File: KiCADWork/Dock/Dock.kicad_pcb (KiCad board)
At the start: 2 copper layers, 166.3 x 101.1 mm, 11 parts, among them J1 Conn_01x10_Pin, J2 Conn_01x10_Pin, U1 MCP73831T-2ACI/OT, U2 XB6096I2SV

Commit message: Dock Updates
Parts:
- removed J2: Conn_01x10_Pin, easyeda2kicad:HDR-TH_10P-P1.27-H-M-R2-C7-S1.27-W7.5-N
- removed U2: XB6096I2SV, easyeda2kicad:WDFN-6_L2.0-W2.0-P0.65-BL-EP
- added BT1: Battery, easyeda2kicad:CONN-TH_S2B-PH-K-LF-SN, B.Cu at (124.1, 52.7)
- added C10: 100n, Capacitor_SMD:C_0402_1005Metric_Pad0.74x0.62mm_HandSolder, F.Cu at (152.9, 61.1)
- added C11: 1u, Capacitor_SMD:C_0402_1005Metric_Pad0.74x0.62mm_HandSolder, F.Cu at (152.9, 63.1)
- added C4: 1u, Capacitor_SMD:C_0402_1005Metric_Pad0.74x0.62mm_HandSolder, F.Cu at (152.9, 53.2)
- added C7: 100n, Capacitor_SMD:C_0402_1005Metric_Pad0.74x0.62mm_HandSolder, F.Cu at (152.9, 55.2)
- added C8: 1u, Capacitor_SMD:C_0402_1005Metric_Pad0.74x0.62mm_HandSolder, F.Cu at (152.9, 57.1)
- added C9: 100n, Capacitor_SMD:C_0402_1005Metric_Pad0.74x0.62mm_HandSolder, F.Cu at (152.9, 59.1)
- added D2: LED, LED_SMD:LED_0603_1608Metric_Pad1.05x0.95mm_HandSolder, F.Cu at (145.1, 51.1)
- added J3: USB_C_Receptacle, easyeda2kicad:USB-C-SMD_TYPEC-952-ACP24, F.Cu at (186.6, 61.1)
- added J4: Conn_01x10_Socket, easyeda2kicad:HDR-TH_10P-P1.27-V-M-R2-C5-S1.27-1, B.Cu at (125.8, 39.1)
- added P1: USB_C_Plug, easyeda2kicad:USB-C-SMD_TYPEC-952-ACP24, F.Cu at (186.6, 44.5)
- added Q1: NTJD4152PT1G, easyeda2kicad:SC-88-6_L2.0-W1.3-P0.65-LS2.1-BL, F.Cu at (156.7, 46.0)
- added R10: 2k, Resistor_SMD:R_0402_1005Metric_Pad0.72x0.64mm_HandSolder, F.Cu at (153.0, 49.1)
- added R11: 2k, Resistor_SMD:R_0402_1005Metric_Pad0.72x0.64mm_HandSolder, F.Cu at (153.0, 51.1)
- added R12: 220, Resistor_SMD:R_0402_1005Metric_Pad0.72x0.64mm_HandSolder, F.Cu at (148.9, 48.2)
- added R13: 220, Resistor_SMD:R_0402_1005Metric_Pad0.72x0.64mm_HandSolder, F.Cu at (148.9, 50.2)
- added R4: 5k1, Resistor_SMD:R_0402_1005Metric_Pad0.72x0.64mm_HandSolder, F.Cu at (159.9, 45.1)
- added R5: 5k1, Resistor_SMD:R_0402_1005Metric_Pad0.72x0.64mm_HandSolder, F.Cu at (159.9, 47.0)
- added R6: 100, Resistor_SMD:R_0402_1005Metric_Pad0.72x0.64mm_HandSolder, F.Cu at (156.2, 53.2)
- added R7: 100, Resistor_SMD:R_0402_1005Metric_Pad0.72x0.64mm_HandSolder, F.Cu at (159.3, 53.2)
- added R8: 100, Resistor_SMD:R_0402_1005Metric_Pad0.72x0.64mm_HandSolder, F.Cu at (153.0, 45.1)
- added R9: 12k 1%, Resistor_SMD:R_0402_1005Metric_Pad0.72x0.64mm_HandSolder, F.Cu at (153.0, 47.1)
- added Y1: X322524MOB4SI, easyeda2kicad:CRYSTAL-SMD_4P-L3.2-W2.5-BL, F.Cu at (157.4, 58.5)
- C1: value 10u -> 18p
- C2: value 100n -> 18p
- C3: value 10u -> 100n
- D1: value WHITE LED -> LED
- J1: value Conn_01x10_Pin -> USB_C_Receptacle; footprint easyeda2kicad:HDR-TH_10P-P1.27-H-M-R2-C7-S1.27-W7.5-N -> easyeda2kicad:TYPE-C-SMD_C9900025773
- R1: value 2k -> 100
- R3: value 2k -> 10k
- U1: value MCP73831T-2ACI/OT -> USB2422T-I/MJ; footprint easyeda2kicad:SOT-23-5_L3.0-W1.7-P0.95-LS2.8-BL -> Temp:QFN-24_L4.0-W4.0-P0.50-TL-EP2.5
- moved J1 43.4 mm to (127.0, 52.8), turned to -90 degrees
- moved D1 24.9 mm to (145.1, 48.5)
- moved U1 5.04 mm to (168.5, 54.6)
- moved R3 1.98 mm to (161.6, 64.3)
- moved R1 1.98 mm to (161.6, 60.4)
- moved R2 1.98 mm to (161.6, 62.3)
- moved C1 1.98 mm to (164.9, 60.3)
- moved C2 1.98 mm to (164.9, 62.3)
- moved C3 1.98 mm to (164.9, 64.3)
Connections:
- C1 pad 1: +BATT -> GND
- C1 pad 2: GND -> Net-(U1-XTALIN/CLKIN)
- C2 pad 1: Net-(U2-VDD) -> Net-(U1-XTALOUT/(CLKIN_EN))
- C2 pad 2: /Charging/BATGND -> GND
- C3 pad 1: /Charging/VBUS -> GND
- C3 pad 2: GND -> +3V3
- D1 pad 1: Net-(D1-K) -> GND
- D1 pad 2: /Charging/VBUS -> Net-(D1-A)
- J1 pad 1: unconnected-(J1-Pin_1-Pad1) -> (no net)
- J1 pad 2: unconnected-(J1-Pin_2-Pad2) -> (no net)
- J1 pad 3: unconnected-(J1-Pin_3-Pad3) -> (no net)
- J1 pad 4: unconnected-(J1-Pin_4-Pad4) -> (no net)
- R1 pad 1: Net-(D1-K) -> Net-(U1-VBUS_DET)
- R1 pad 2: Net-(U1-STAT) -> VTRef
- R2 pad 1: Net-(U2-VDD) -> GND
- R2 pad 2: +BATT -> Net-(U1-VBUS_DET)
- R3 pad 1: Net-(U1-PROG) -> RESET
- R3 pad 2: GND -> +3V3
- U1 pad 1: Net-(U1-STAT) -> +3V3
- U1 pad 2: GND -> /DeviceSelect/D1-
- U1 pad 3: +BATT -> /DeviceSelect/D1+
- U1 pad 4: /Charging/VBUS -> /DeviceSelect/D2-
- U1 pad 5: Net-(U1-PROG) -> /DeviceSelect/D2+
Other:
- board size 166.3 x 101.1 mm -> 70.5 x 35.5 mm

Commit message: Ignoring Backups
More Dock progress
All local backups removed
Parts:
- removed BT1: Battery, easyeda2kicad:CONN-TH_S2B-PH-K-LF-SN
- removed J3: USB_C_Receptacle, easyeda2kicad:USB-C-SMD_TYPEC-952-ACP24
- added BT2: Battery, easyeda2kicad:CONN-TH_S2B-PH-K-LF-SN, B.Cu at (124.1, 52.7)
- added C12: 4.7u, Capacitor_SMD:C_0402_1005Metric_Pad0.74x0.62mm_HandSolder, F.Cu at (115.2, 37.4)
- added C13: 2.2u, Capacitor_SMD:C_0402_1005Metric_Pad0.74x0.62mm_HandSolder, F.Cu at (143.8, 21.6)
- added C14: 2.2u, Capacitor_SMD:C_0402_1005Metric_Pad0.74x0.62mm_HandSolder, F.Cu at (131.0, 21.7)
- added C15: 10u, Capacitor_SMD:C_0402_1005Metric_Pad0.74x0.62mm_HandSolder, F.Cu at (100.6, 77.5)
- added C16: 22u, Capacitor_SMD:C_0603_1608Metric_Pad1.08x0.95mm_HandSolder, F.Cu at (96.9, 78.5)
- added C17: 22u, Capacitor_SMD:C_0603_1608Metric_Pad1.08x0.95mm_HandSolder, F.Cu at (96.9, 81.0)
- added C5: 1u, Capacitor_SMD:C_0402_1005Metric_Pad0.74x0.62mm_HandSolder, F.Cu at (107.9, 30.8)
- added C6: 4.7u, Capacitor_SMD:C_0402_1005Metric_Pad0.74x0.62mm_HandSolder, F.Cu at (115.2, 35.4)
- added D3: BLUE LED, LED_SMD:LED_0603_1608Metric_Pad1.05x0.95mm_HandSolder, F.Cu at (110.6, 26.7)
- added D4: BLUE RED, LED_SMD:LED_0603_1608Metric_Pad1.05x0.95mm_HandSolder, F.Cu at (104.0, 29.0)
- added L1: 4.7u, easyeda2kicad:IND-SMD_L5.2-W5.2_YSPI0530, F.Cu at (95.3, 73.7)
- added P2: USB_C_Plug, easyeda2kicad:USB-C-SMD_918-118A2021S40003, F.Cu at (191.8, 65.3)
- added R14: 1.78k, Resistor_SMD:R_0402_1005Metric_Pad0.72x0.64mm_HandSolder, F.Cu at (98.9, 28.6)
- added R15: 1.18k, Resistor_SMD:R_0402_1005Metric_Pad0.72x0.64mm_HandSolder, F.Cu at (98.9, 30.6)
- added R16: 1.18k, Resistor_SMD:R_0402_1005Metric_Pad0.72x0.64mm_HandSolder, F.Cu at (98.9, 32.6)
- added R17: 1.18k, Resistor_SMD:R_0402_1005Metric_Pad0.72x0.64mm_HandSolder, F.Cu at (104.1, 31.5)
- added R18: 10k, Resistor_SMD:R_0402_1005Metric_Pad0.72x0.64mm_HandSolder, F.Cu at (107.7, 39.1)
- added R19: 100k, Resistor_SMD:R_0402_1005Metric_Pad0.72x0.64mm_HandSolder, F.Cu at (104.5, 78.1)
- added R20: 732, Resistor_SMD:R_0402_1005Metric_Pad0.72x0.64mm_HandSolder, F.Cu at (104.5, 80.1)
- added U2: TPS61023DRLR, easyeda2kicad:SOT-563_L1.6-W1.2-P0.50-LS1.6-BR, F.Cu at (100.6, 79.4)
- added U3: AMS1117-3.3, Package_TO_SOT_SMD:SOT-223-3_TabPin2, F.Cu at (137.2, 20.9)
- added U4: BQ24073RGT, Package_DFN_QFN:VQFN-16-1EP_3x3mm_P0.5mm_EP1.6x1.6mm, F.Cu at (108.7, 35.5)
- D1, D2: value LED -> BLUE LED
- P1: footprint easyeda2kicad:USB-C-SMD_TYPEC-952-ACP24 -> easyeda2kicad:USB-C-SMD_918-118A2021S40003
- R9: value 12k 1% -> 12k
- moved P1 65.9 mm to (124.0, 65.4), turned to -90 degrees
- moved R8 63.8 mm to (215.5, 32.0)
- moved R9 63.8 mm to (215.5, 34.0)
- moved C10 57.4 mm to (205.7, 38.3)
- moved C11 57.4 mm to (205.7, 40.3)
- moved C4 57.4 mm to (205.6, 30.4)
- moved C7 57.4 mm to (205.7, 32.4)
- moved C8 57.4 mm to (205.7, 34.4)
- moved C9 57.4 mm to (205.7, 36.3)
- moved R1 57.4 mm to (214.3, 37.6)
- moved R2 57.4 mm to (214.3, 39.5)
- moved R3 57.4 mm to (214.3, 41.5)
- moved U1 57.4 mm to (221.2, 31.8)
- moved Y1 57.4 mm to (210.1, 35.7)
- moved C1 57.4 mm to (217.6, 37.5)
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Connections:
- J1 pad A7: /DeviceSelect/D- -> /DeviceSelect/D+
- J1 pad B10: unconnected-(J1-RX1--PadB10) -> /DeviceSelect/D+
- J1 pad B11: unconnected-(J1-RX1+-PadB11) -> /DeviceSelect/D+
- J1 pad B7: /DeviceSelect/D- -> /DeviceSelect/D+
- Q1 pad 1: VTRef -> /DeviceSelect/VBus
- Q1 pad 4: VTRef -> /DeviceSelect/VBus
- R1 pad 2: VTRef -> /DeviceSelect/Vsys
- R10 pad 1: VTRef -> /DeviceSelect/VBus
- R11 pad 1: VTRef -> /DeviceSelect/VBus
- U1 pad 19: /DeviceSelect/D- -> /DeviceSelect/D+

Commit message: Beautiful Skilkscreen Added
Dock schematic intial draft complete
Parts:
- added D5: LED, LED_SMD:LED_0603_1608Metric_Pad1.05x0.95mm_HandSolder, F.Cu at (131.1, 24.8)
- added R21: 2k, Resistor_SMD:R_0402_1005Metric_Pad0.72x0.64mm_HandSolder, F.Cu at (128.5, 22.3)
- added TP1: TestPoint, TestPoint:TestPoint_Pad_D1.0mm, F.Cu at (173.3, 21.7)
- added TP10: TestPoint, TestPoint:TestPoint_Pad_D1.0mm, F.Cu at (187.5, 26.9)
- added TP11: TestPoint, TestPoint:TestPoint_Pad_D1.0mm, F.Cu at (91.2, 42.7)
- added TP12: TestPoint, TestPoint:TestPoint_Pad_D1.0mm, F.Cu at (91.2, 45.7)
- added TP13: TestPoint, TestPoint:TestPoint_Pad_D1.0mm, F.Cu at (91.2, 48.8)
- added TP14: TestPoint, TestPoint:TestPoint_Pad_D1.0mm, F.Cu at (91.2, 51.8)
- added TP15: TestPoint, TestPoint:TestPoint_Pad_D1.0mm, F.Cu at (94.3, 42.7)
- added TP16: TestPoint, TestPoint:TestPoint_Pad_D1.0mm, F.Cu at (94.3, 45.7)
- added TP17: TestPoint, TestPoint:TestPoint_Pad_D1.0mm, F.Cu at (94.3, 48.8)
- added TP2: TestPoint, TestPoint:TestPoint_Pad_D1.0mm, F.Cu at (176.4, 21.7)
- added TP3: TestPoint, TestPoint:TestPoint_Pad_D1.0mm, F.Cu at (181.4, 21.7)
- added TP4: TestPoint, TestPoint:TestPoint_Pad_D1.0mm, F.Cu at (184.5, 21.7)
- added TP5: TestPoint, TestPoint:TestPoint_Pad_D1.0mm, F.Cu at (187.5, 21.7)
- added TP6: TestPoint, TestPoint:TestPoint_Pad_D1.0mm, F.Cu at (175.3, 26.9)
- added TP7: TestPoint, TestPoint:TestPoint_Pad_D1.0mm, F.Cu at (178.4, 26.9)
- added TP8: TestPoint, TestPoint:TestPoint_Pad_D1.0mm, F.Cu at (181.4, 26.9)
- added TP9: TestPoint, TestPoint:TestPoint_Pad_D1.0mm, F.Cu at (184.5, 26.9)
- R1, R2: value 100 -> 10k
- moved U4 80.1 mm to (188.7, 39.5)

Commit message: Small Updates
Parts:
- D3, D4: footprint LED_SMD:LED_0603_1608Metric_Pad1.05x0.95mm_HandSolder -> easyeda2kicad:SideStuckLED
- P1, P2: footprint easyeda2kicad:USB-C-SMD_918-118A2021S40003 -> easyeda2kicad:USB-C-SMD_TYPE-C-24P-GTJB-040
- moved D4 73.9 mm to (177.5, 20.9)
- moved TP2 72.6 mm to (236.6, 62.2)
- moved TP4 72.6 mm to (244.7, 62.2)
- moved TP6 72.6 mm to (235.5, 67.5)
- moved TP8 72.6 mm to (241.6, 67.5)
- moved TP1 72.6 mm to (233.5, 62.2)
- moved TP10 72.6 mm to (247.7, 67.5)
- moved TP3 72.6 mm to (241.6, 62.2)
- moved TP5 72.6 mm to (247.7, 62.2)
- moved TP7 72.6 mm to (238.6, 67.5)
- moved TP9 72.6 mm to (244.7, 67.5)
- moved C14 66.1 mm to (70.8, 49.0)
- moved D5 66.1 mm to (70.9, 52.1)
- moved R21 66.1 mm to (68.3, 49.6)
- moved C13 66.1 mm to (83.6, 48.9)
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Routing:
- net GND: track 0.00 -> 11.5 mm, vias 0 -> 10
- net Net-(D4-K): track 0.00 -> 3.85 mm
- net Net-(U2-EN): track 0.00 -> 2.80 mm
- net Net-(D4-A): track 0.00 -> 1.68 mm
- net VTRef: track 0.00 -> 1.63 mm
- net Net-(U4-ISET): track 0.00 -> 1.61 mm
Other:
- board size 70.5 x 35.5 mm -> 78.5 x 49.6 mm

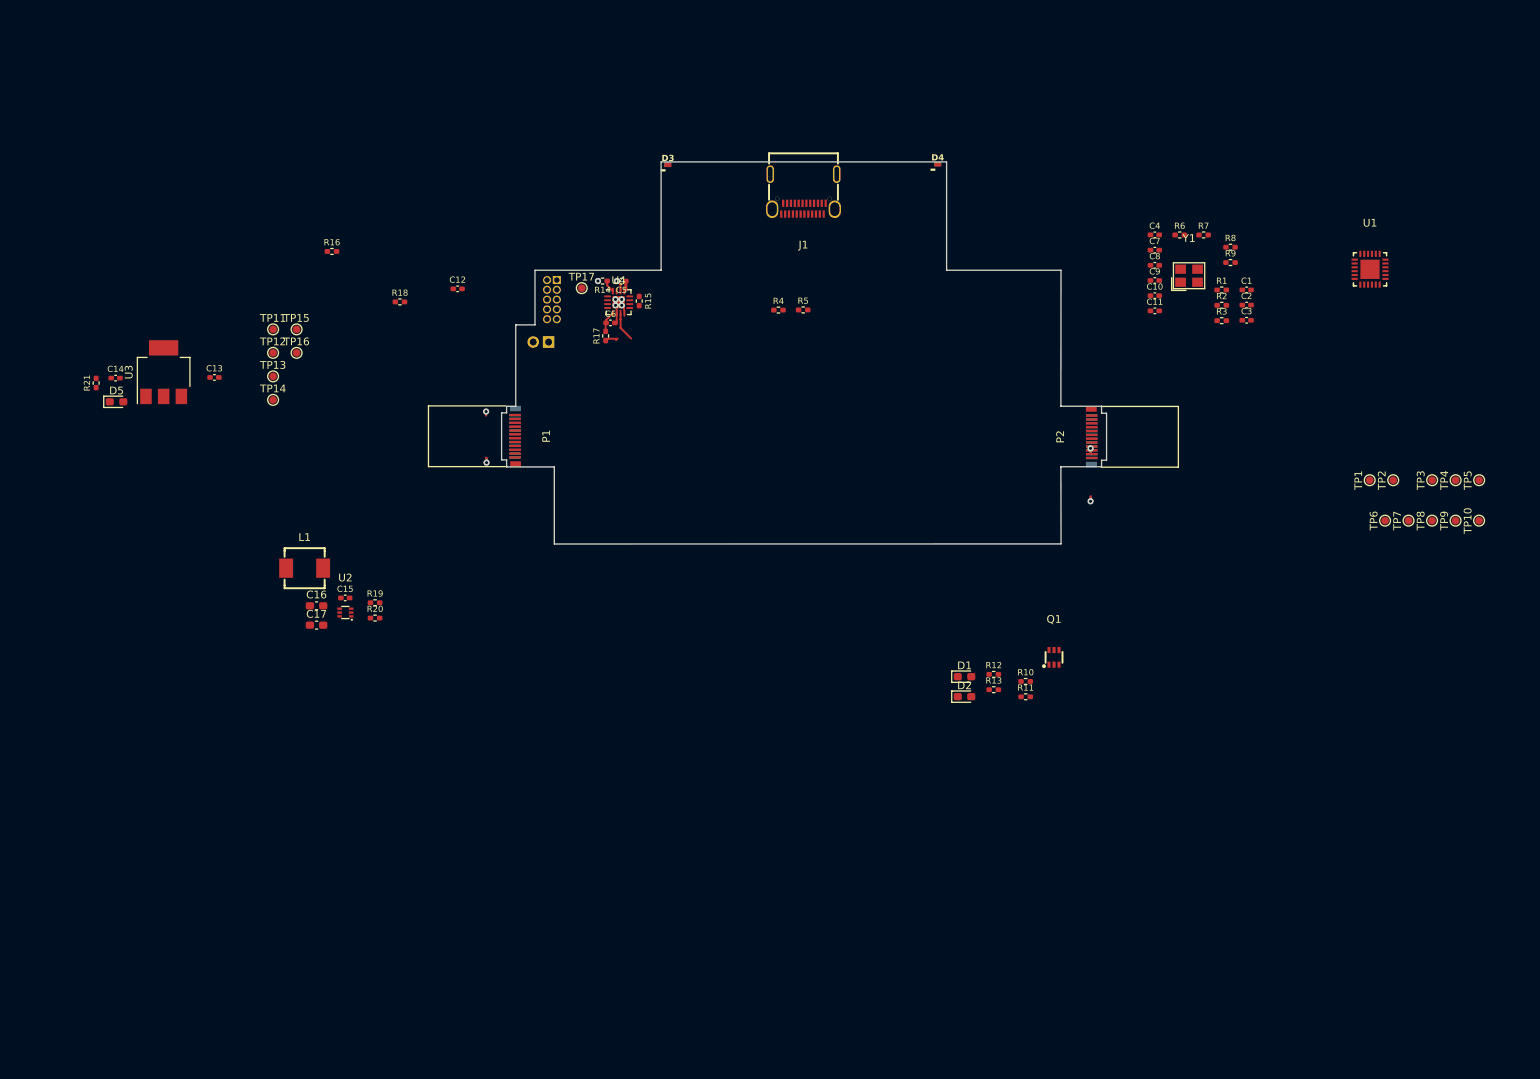
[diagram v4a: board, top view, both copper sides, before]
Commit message: Dock Updates
Starting to layout the dock
Dom still to check
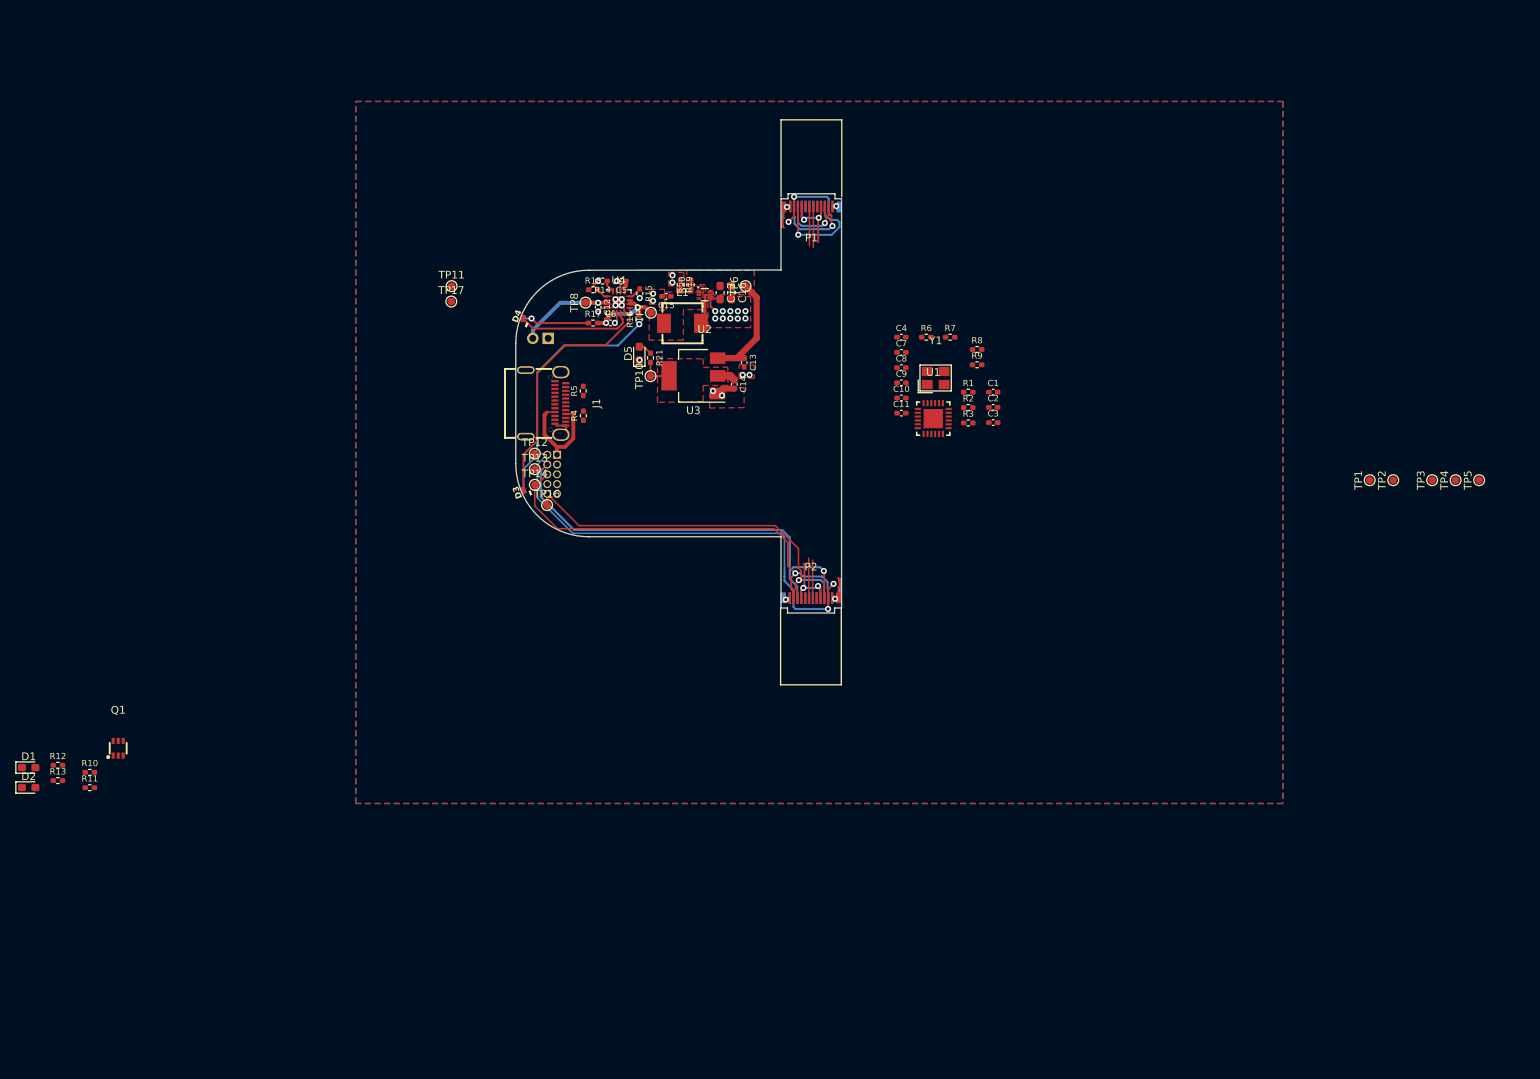
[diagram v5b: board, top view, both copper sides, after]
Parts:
- removed TP15, TP9: TestPoint, TestPoint:TestPoint_Pad_D1.0mm
- moved D1 122.0 mm to (59.5, 99.5)
- moved D2 122.0 mm to (59.5, 102.1)
- moved Q1 122.0 mm to (71.1, 97.0)
- moved R10 122.0 mm to (67.5, 100.2)
- moved R11 122.0 mm to (67.5, 102.1)
- moved R12 122.0 mm to (63.3, 99.2)
- moved R13 122.0 mm to (63.3, 101.2)
- moved TP8 113.4 mm to (131.8, 39.2)
- moved TP10 109.1 mm to (140.2, 48.7)
- moved TP7 101.9 mm to (140.3, 40.5)
- moved TP6 88.4 mm to (152.5, 37.1)
- moved C14 80.3 mm to (151.1, 49.8), turned to -90 degrees
- moved R21 72.0 mm to (140.2, 46.4), turned to -90 degrees
- moved C13 68.8 mm to (152.4, 47.0), turned to -90 degrees
- moved U3 68.7 mm to (145.8, 48.7), turned to 180 degrees
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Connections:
- net Net-(BT2-+) renamed /ExtraBattery/VBAT
- C15 pad 1: Net-(U2-EN) -> /ExtraBattery/3.7Out
- C6 pad 1: Net-(U2-EN) -> /ExtraBattery/3.7Out
- J4 pad 3: Net-(J4-Pin_3) -> GND
- J4 pad 5: Net-(J4-Pin_3) -> GND
- J4 pad 6: nRESET -> SWO
- J4 pad 8: TDI -> unconnected-(J4-Pin_8-Pad8)
- L1 pad 1: Net-(U2-VIN) -> /ExtraBattery/3.7Out
- L1 pad 2: Net-(U2-EN) -> Net-(U2-SW)
- P1 pad A3: SWDCLK -> SWCLK
- P1 pad B3: SWDCLK -> SWCLK
- P2 pad A3: SWDCLK -> SWCLK
- P2 pad B3: SWDCLK -> SWCLK
- R16 pad 2: Net-(U2-EN) -> /ExtraBattery/3.7Out
- R17 pad 2: Net-(U2-EN) -> /ExtraBattery/3.7Out
- R19 pad 2: /DeviceSelect/Vsys -> /ExtraBattery/FB
- R20 pad 1: Net-(U2-FB) -> /ExtraBattery/FB
- TP14 pad 1: nRESET -> SWO
- TP17 pad 1: Net-(J4-Pin_3) -> GND
- TP7 pad 1: Net-(U2-EN) -> /ExtraBattery/3.7Out
- U2 pad 1: Net-(U2-FB) -> /ExtraBattery/FB
- U2 pad 2: Net-(U2-EN) -> /ExtraBattery/3.7Out
- U2 pad 3: Net-(U2-VIN) -> /ExtraBattery/3.7Out
- U2 pad 5: Net-(U2-EN) -> Net-(U2-SW)
- U4 pad 10: Net-(U2-EN) -> /ExtraBattery/3.7Out
- U4 pad 11: Net-(U2-EN) -> /ExtraBattery/3.7Out
- U4 pad 5: Net-(U2-EN) -> /ExtraBattery/3.7Out
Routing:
- net SWCLK: track 0.00 -> 71.2 mm, vias 0 -> 2
- net SWDIO: track 0.00 -> 70.0 mm, vias 0 -> 4
- net SWO: track 0.00 -> 66.1 mm, vias 0 -> 2
- net nRESET: track 0.00 -> 57.5 mm, vias 0 -> 2
- net Net-(D3-K): track 0.00 -> 32.4 mm
- net Net-(D3-A): track 0.00 -> 31.9 mm, vias 0 -> 1
- net GND: track 11.5 -> 34.9 mm, vias 10 -> 32
- net VTRef: track 1.63 -> 16.8 mm
- net /DeviceSelect/Vsys: track 0.00 -> 14.5 mm
- net /ExtraBattery/VBAT: track 0.00 -> 14.2 mm, vias 0 -> 1
- net /ExtraBattery/3.7Out: track 0.00 -> 14.2 mm, vias 0 -> 2
- net /DeviceSelect/VBUS2: track 0.00 -> 12.2 mm, vias 0 -> 2
- net /DeviceSelect/VBUS1: track 0.00 -> 12.1 mm, vias 0 -> 2
- net Net-(D4-K): track 3.85 -> 15.2 mm
- net Net-(D4-A): track 1.68 -> 8.73 mm, vias 0 -> 1
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- added copper zone on F.Cu, net +3V3
- added copper zone on F.Cu, net /DeviceSelect/Vsys
- added copper zone on F.Cu, net /ExtraBattery/3.7Out
- added copper zone on F.Cu, net /ExtraBattery/FB
- added copper zone on B.Cu, net GND
- added copper zone on F.Cu, net GND
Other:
- board size 78.5 x 49.6 mm -> 42.3 x 54.4 mm
